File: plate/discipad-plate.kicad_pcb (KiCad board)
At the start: 2 copper layers, 76.3 x 95.2 mm, 0 parts

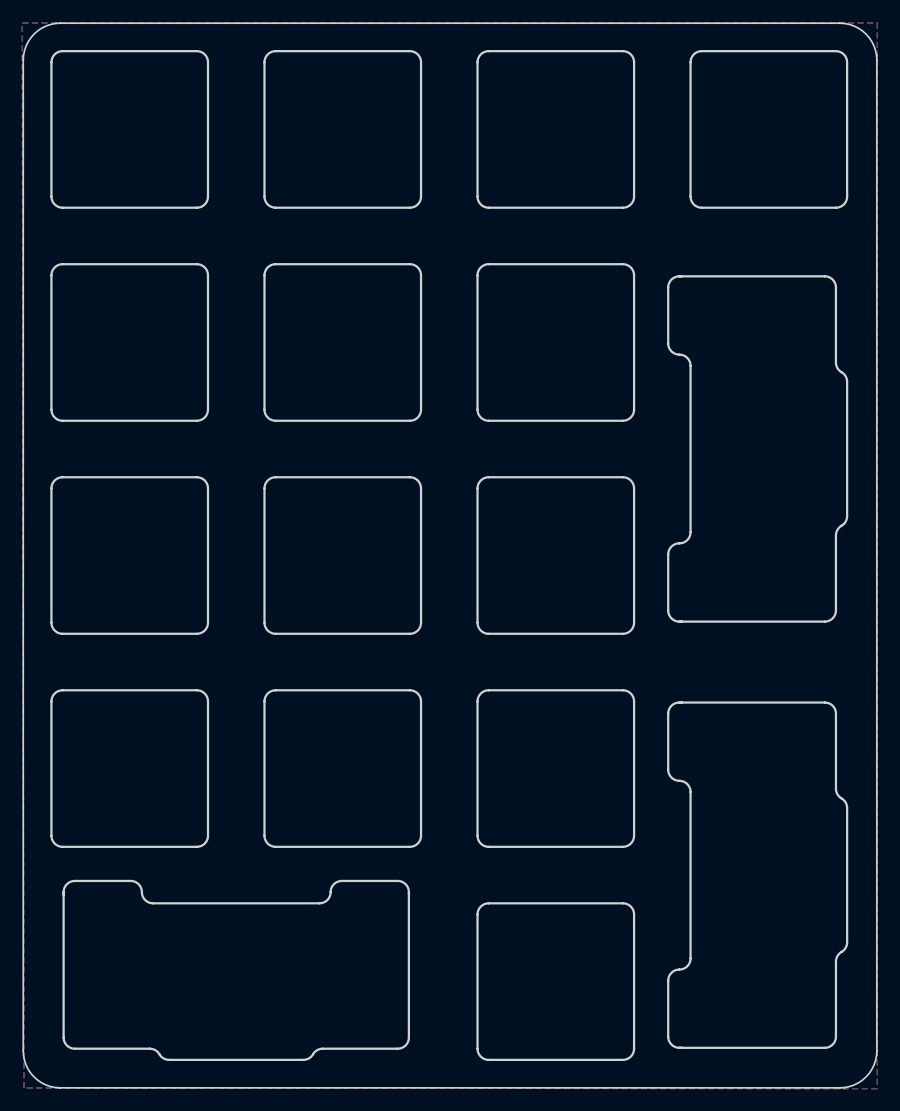
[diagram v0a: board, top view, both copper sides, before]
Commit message: Update plate with JLCPCB order placeholder
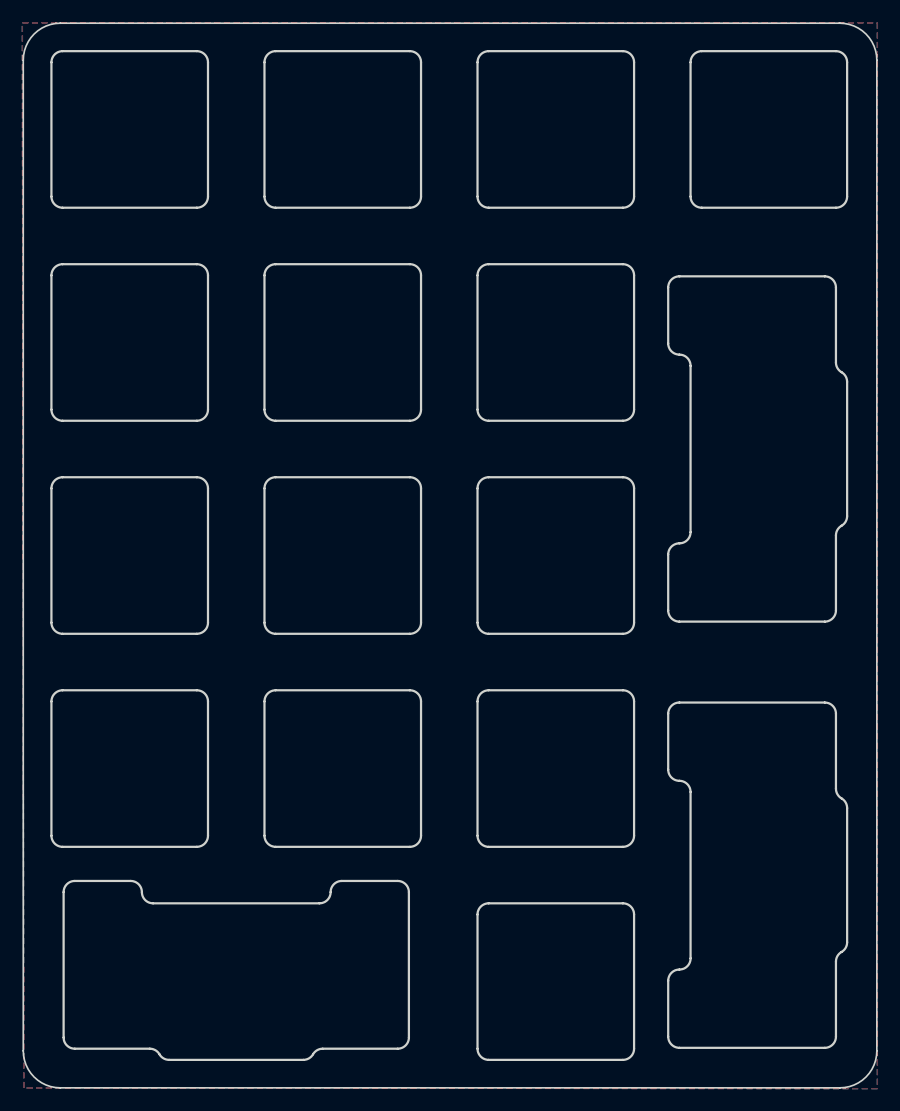
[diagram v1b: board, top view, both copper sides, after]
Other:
- outline, holes or cut-outs redrawn
- board text added: "Discipad plate by piit79 of 42keebs.eu"
- board text added: "JLCJLCJLCJLC"
- board text removed: "Discipad plate by piit79 2021"

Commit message: Plate RevC: update with split 2u keys
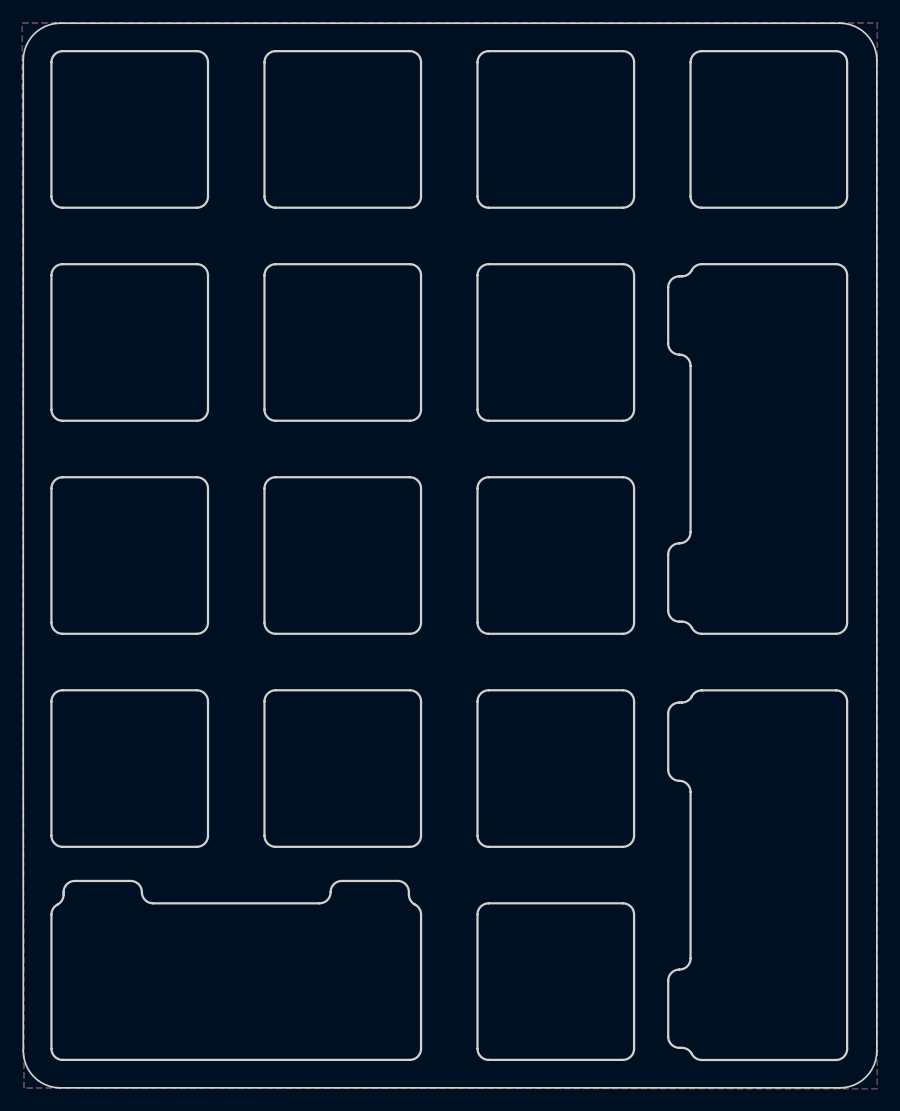
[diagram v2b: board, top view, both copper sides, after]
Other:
- outline, holes or cut-outs redrawn
- net class Default removed
- board text added: "Discipad RevC plate by piit79 / 42keebs.eu"
- board text removed: "Discipad plate by piit79 of 42keebs.eu"
